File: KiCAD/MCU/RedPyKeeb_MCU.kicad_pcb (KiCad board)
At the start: 4 copper layers, 90.2 x 83.8 mm, 22 parts, among them J0 Conn_01x04, J1 Conn_01x36, J2 Conn_01x04, U1 MCP23S17-E/SO, U2 MCP23S17-E/SO, U3 TXB0104D, U4 TXB0104D, U5 TXS0104ED, U6 SN74HC595DW, U7 TXS0104ED

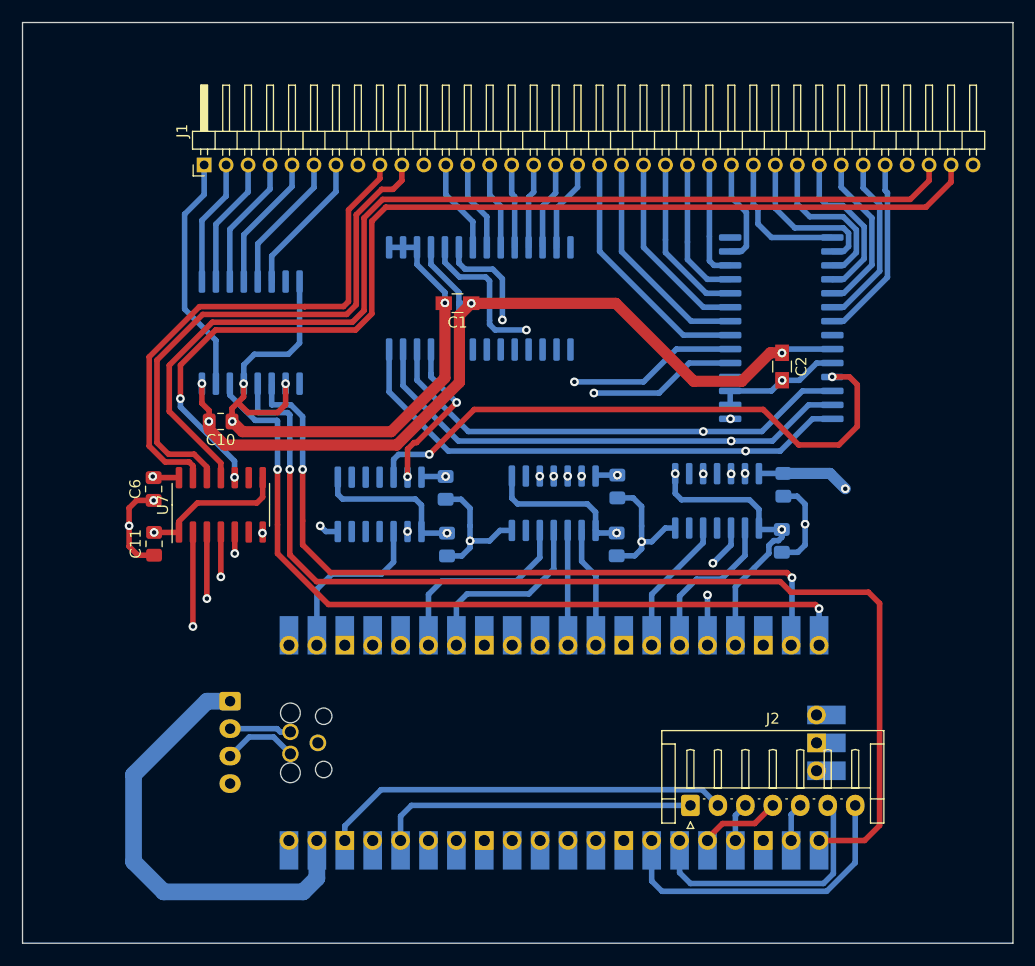
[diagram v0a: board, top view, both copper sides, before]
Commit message: This is as-is before I test out a teensy MCU instead of the pico..
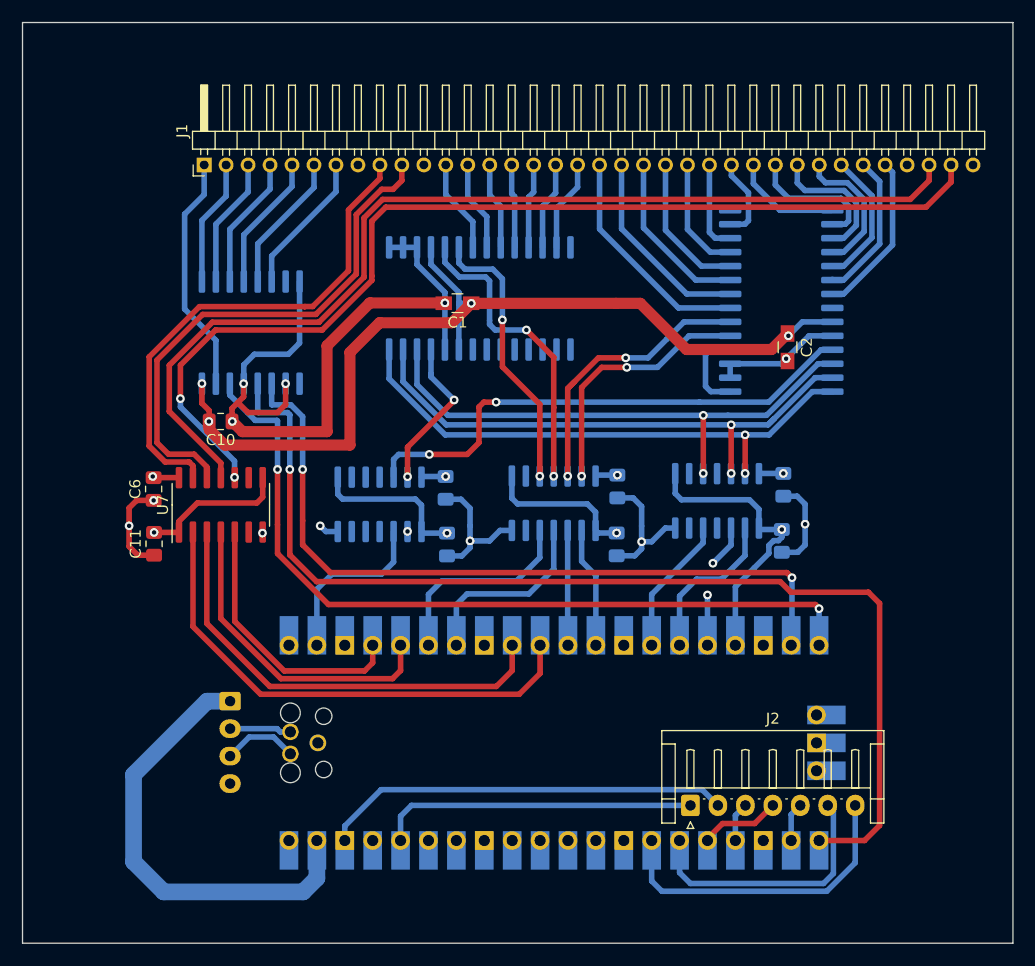
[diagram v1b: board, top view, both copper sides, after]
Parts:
- moved U2 2.48 mm to (108.4, 50.7)
- moved C2 1.82 mm to (109.0, 55.0)
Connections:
- U1 pad 1: KEY_ROW0 -> Net-(U1-Pad1)
- U1 pad 2: KEY_ROW1 -> Net-(U1-Pad2)
- U1 pad 3: KEY_ROW2 -> Net-(U1-Pad3)
- U1 pad 4: KEY_ROW3 -> Net-(U1-Pad4)
- U1 pad 5: KEY_ROW4 -> Net-(U1-Pad5)
- U1 pad 6: KEY_ROW5 -> Net-(U1-Pad6)
- U1 pad 7: KEY_ROW6 -> Net-(U1-Pad7)
- U2 pad 15: PICO_33_REF -> MAIN_VBUS
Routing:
- net MAIN_VBUS: track 480.9 -> 390.4 mm
- net PICO_33_REF: track 140.9 -> 130.9 mm, vias 6 -> 4
- net IO_CS1: track 54.1 -> 47.6 mm
- net KEY_COL14: track 12.8 -> 9.90 mm
- net KEY_COL11: track 13.2 -> 10.6 mm
- net KEY_COL12: track 10.8 -> 8.25 mm
- net KEY_COL18: track 14.9 -> 12.5 mm
- net KEY_COL19: track 16.0 -> 13.5 mm
- net KEY_COL8: track 20.4 -> 18.2 mm
- net KEY_COL7: track 22.9 -> 20.7 mm
- net KEY_COL10: track 15.4 -> 13.2 mm
- net KEY_COL15: track 14.4 -> 12.3 mm
- net KEY_COL17: track 14.8 -> 12.6 mm
- net KEY_COL16: track 14.7 -> 12.5 mm
- net KEY_COL13: track 9.72 -> 7.58 mm
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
